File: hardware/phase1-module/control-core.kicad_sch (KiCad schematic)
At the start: 17 parts, among them U1 DAC80502, U2 OPA2189

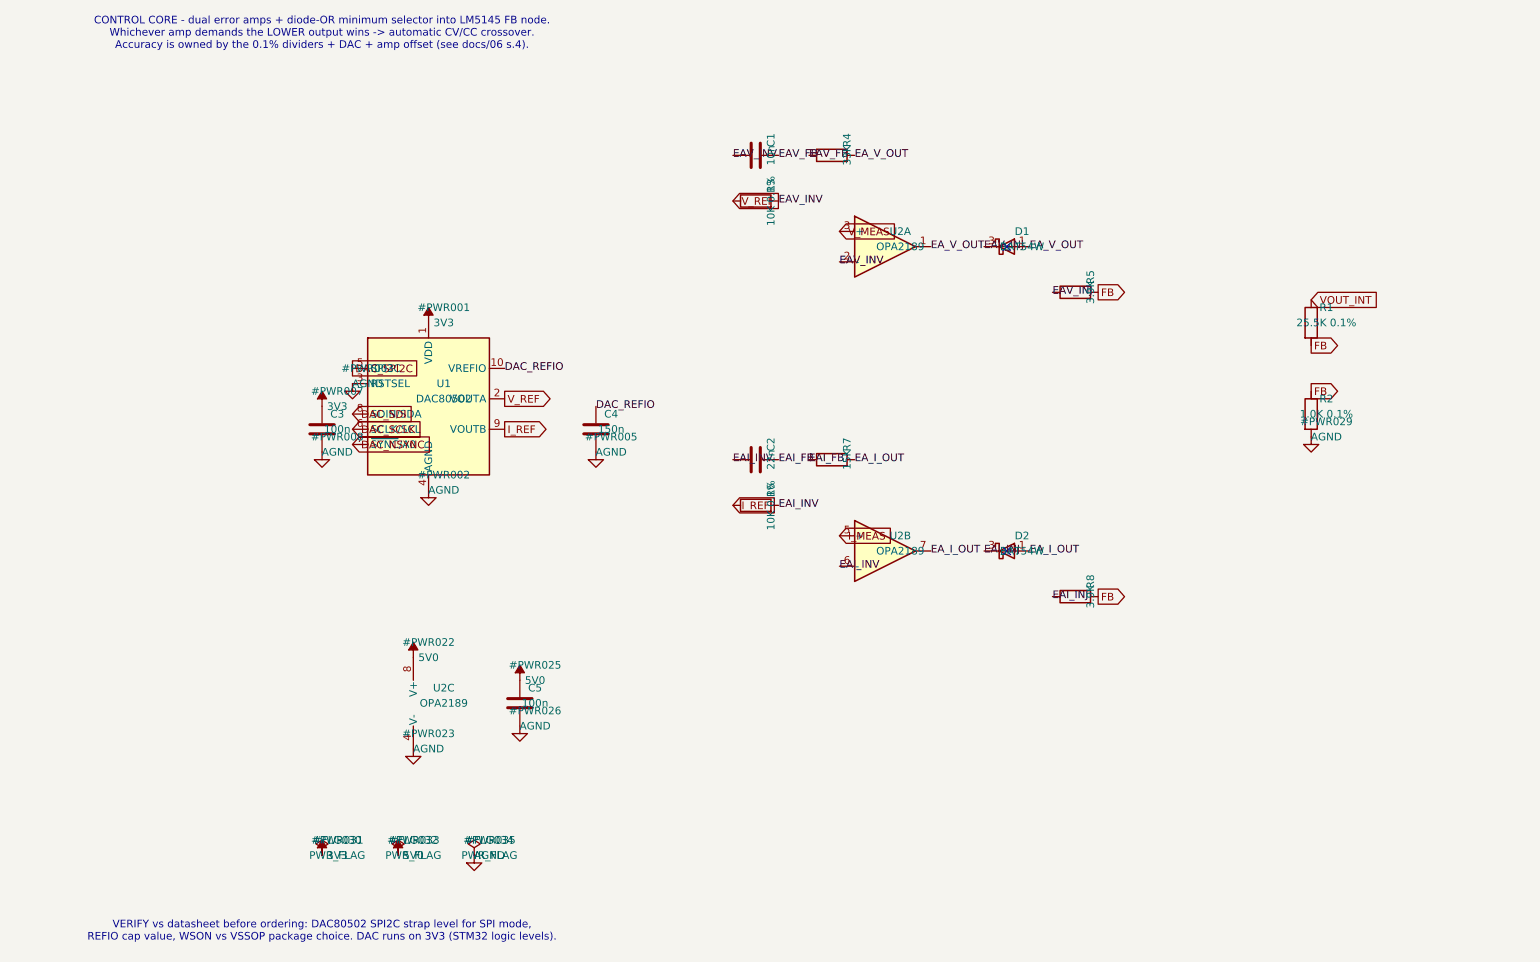
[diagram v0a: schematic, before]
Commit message: control-core sheet: verified generation, wired runs, clean field placement
- kicad_gen: pin-bbox-based Reference/Value placement, wire support,
  outward-rotated labels, synthesized power ports, hidden flag text
- gen_phase1: control-core rows rewired (op-amp -> diode-OR -> injection
  as real wires with on-wire labels), collision fixes, DAC decoupling moved
- Netlist assertions pass 22/22 (check_netlist.py); render inspected
- docs/06: DAC80502 moved to 3V3 rail (STM32 logic levels), BAT54W SC-70
  pinout notes

Co-Authored-By: Claude Fable 5 <noreply@anthropic.com>
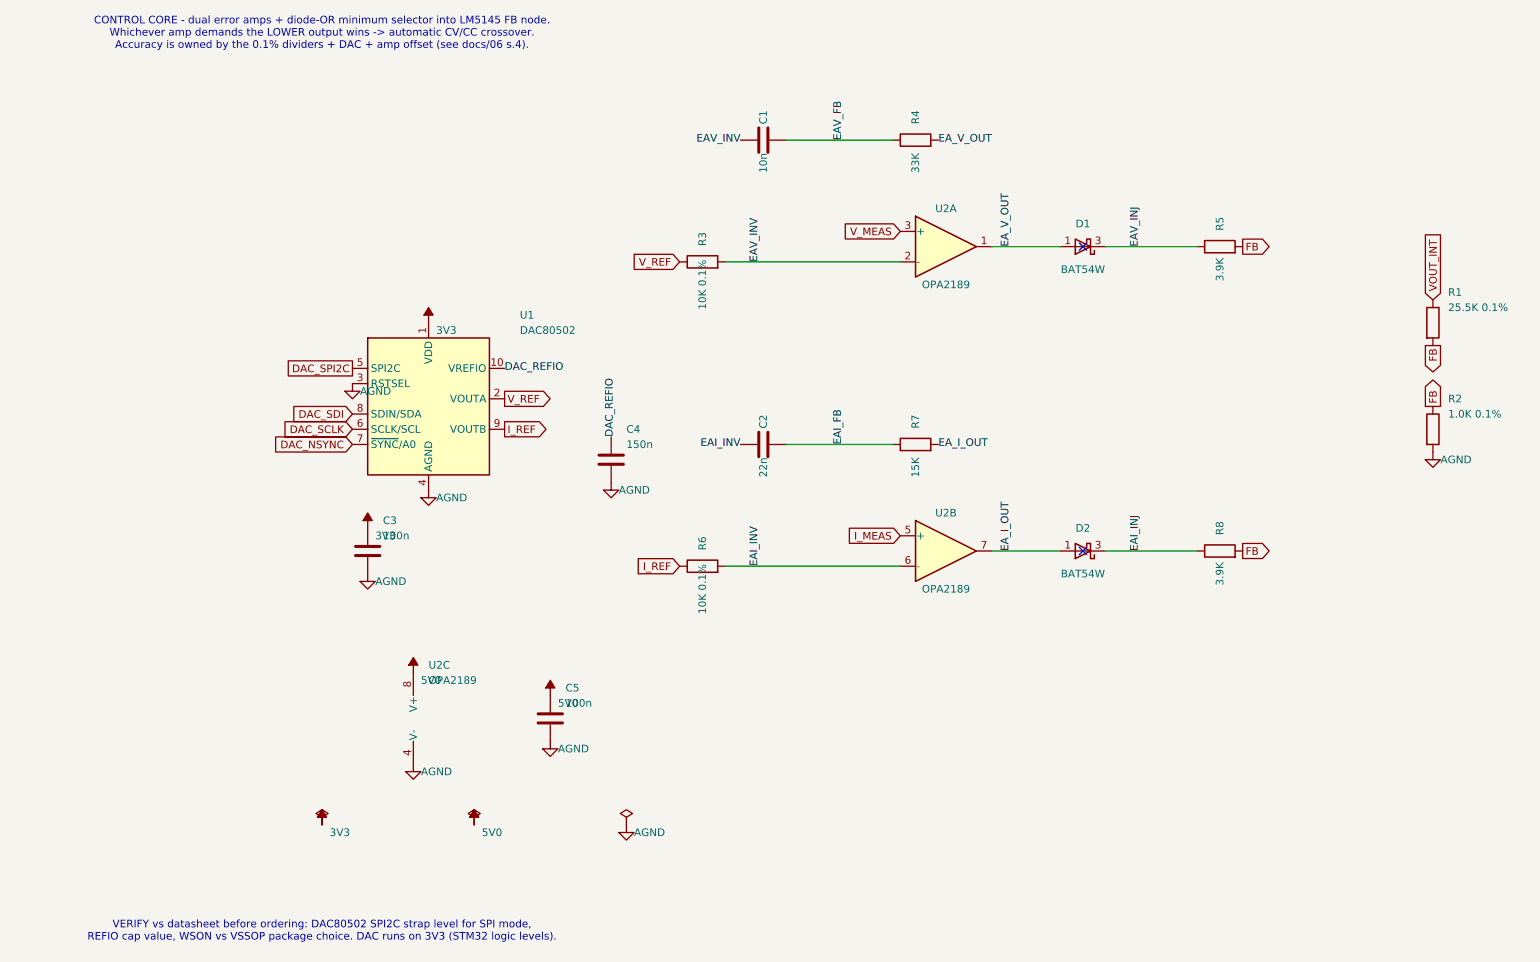
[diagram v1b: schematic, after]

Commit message: Two part disqualifications caught by exact-variant spec check
- OPA2189 -> OPA2333: OPAx189 input common-mode range stops ~2.5V below
  V+, colliding with our 2.5V full-scale signals on the 5V rail
- TPS54202 -> LMR36015: 28V Vin(max) is inside the 24-30V bus spec;
  60V part restores margin
- DAC80502 footprint pinned to VSSOP-10 (DGS), exact orderables for all
  section-B parts in PARTS-TO-DOWNLOAD.md (incl. STM32G431CBT6 + RM0440)

Co-Authored-By: Claude Fable 5 <noreply@anthropic.com>
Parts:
- U1: footprint Package_SON:WSON-10-1EP_2.5x2.5mm_P0.5mm -> Package_SO:VSSOP-10_3x3mm_P0.5mm
- U2: value OPA2189 -> OPA2333
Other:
- note added: "VERIFY vs datasheet before ordering: DAC80502 SPI2C strap level for SPI mode, REFIO cap value. Package: VSSOP-10 (DGS). DAC runs on 3V3 (STM32 logic levels). EAs: OPA2333 (RRIO; OPA2189 rejected - input CM stops 2.5V below V+)."
- note removed: "VERIFY vs datasheet before ordering: DAC80502 SPI2C strap level for SPI mode, REFIO cap value, WSON vs VSSOP package choice. DAC runs on 3V3 (STM32 logic levels)."
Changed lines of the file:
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@@
   (global_label "FB" (shape output) (at 218.44 102.87 90) (fields_autoplaced) (effects (font (size 1.27 1.27))))
   (text "CONTROL CORE - dual error amps + diode-OR minimum selector into LM5145 FB node.\nWhichever amp demands the LOWER output wins -> automatic CV/CC crossover.\nAccuracy is owned by the 0.1% dividers + DAC + amp offset (see docs/06 s.4)." (at 33.02 40.64 0) (effects (font (size 1.27 1.27))))
-  (text "VERIFY vs datasheet before ordering: DAC80502 SPI2C strap level for SPI mode,\nREFIO cap value, WSON vs VSSOP package choice. DAC runs on 3V3 (STM32 logic levels)." (at 33.02 190.5 0) (effects (font (size 1.27 1.27))))
+  (text "VERIFY vs datasheet before ordering: DAC80502 SPI2C strap level for SPI mode,\nREFIO cap value. Package: VSSOP-10 (DGS). DAC runs on 3V3 (STM32 logic levels).\nEAs: OPA2333 (RRIO; OPA2189 rejected - input CM stops 2.5V below V+)." (at 33.02 190.5 0) (effects (font (size 1.27 1.27))))
   (symbol (lib_id "Analog_DAC:DAC80502") (at 50.8 101.6 0) (unit 1)
     (in_bom yes) (on_board yes) (dnp no)
     (property "Reference" "U1" (at 66.04 87.63000000000001 0) (effects (font (size 1.27 1.27)) (justify left)))
     (property "Value" "DAC80502" (at 66.04 90.17 0) (effects (font (size 1.27 1.27)) (justify left)))
-    (property "Footprint" "Package_SON:WSON-10-1EP_2.5x2.5mm_P0.5mm" (at 50.8 101.6 0) (effects (font (size 1.27 1.27)) hide))
+    (property "Footprint" "Package_SO:VSSOP-10_3x3mm_P0.5mm" (at 50.8 101.6 0) (effects (font (size 1.27 1.27)) hide))
     (property "Datasheet" "~" (at 50.8 101.6 0) (effects (font (size 1.27 1.27)) hide))
     (pin "1")
@@
     (in_bom yes) (on_board yes) (dnp no)
     (property "Reference" "U2" (at 137.16 69.85 0) (effects (font (size 1.27 1.27))))
-    (property "Value" "OPA2189" (at 137.16 82.55 0) (effects (font (size 1.27 1.27))))
+    (property "Value" "OPA2333" (at 137.16 82.55 0) (effects (font (size 1.27 1.27))))
     (property "Footprint" "Package_SO:VSSOP-8_3x3mm_P0.65mm" (at 137.16 76.2 0) (effects (font (size 1.27 1.27)) hide))
     (property "Datasheet" "~" (at 137.16 76.2 0) (effects (font (size 1.27 1.27)) hide))
@@
     (in_bom yes) (on_board yes) (dnp no)
     (property "Reference" "U2" (at 137.16 120.64999999999999 0) (effects (font (size 1.27 1.27))))
-    (property "Value" "OPA2189" (at 137.16 133.35 0) (effects (font (size 1.27 1.27))))
+    (property "Value" "OPA2333" (at 137.16 133.35 0) (effects (font (size 1.27 1.27))))
     (property "Footprint" "Package_SO:VSSOP-8_3x3mm_P0.65mm" (at 137.16 127.0 0) (effects (font (size 1.27 1.27)) hide))
     (property "Datasheet" "~" (at 137.16 127.0 0) (effects (font (size 1.27 1.27)) hide))
@@
     (in_bom yes) (on_board yes) (dnp no)
     (property "Reference" "U2" (at 50.8 146.04999999999998 0) (effects (font (size 1.27 1.27)) (justify left)))
-    (property "Value" "OPA2189" (at 50.8 148.59 0) (effects (font (size 1.27 1.27)) (justify left)))
+    (property "Value" "OPA2333" (at 50.8 148.59 0) (effects (font (size 1.27 1.27)) (justify left)))
     (property "Footprint" "Package_SO:VSSOP-8_3x3mm_P0.65mm" (at 50.8 154.94 0) (effects (font (size 1.27 1.27)) hide))
     (property "Datasheet" "~" (at 50.8 154.94 0) (effects (font (size 1.27 1.27)) hide))

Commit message: DAC80502 straps verified and applied; two package corrections
- SPI2C strapped to AGND (low = SPI mode, ds 8.5.1); RSTSEL low =
  zero-code POR confirmed - both now hardwired in control-core
- DAC80502 is WSON-10 (DRX) only; VSSOP/DGS was the DAC80501 single.
  Footprint reverted, Value = DAC80502DRXT
- LMR36015 is VQFN-HR-12 (RNX), not HSOIC-8; AQRNXRQ1 variant vetted
  (adjustable, 400 kHz, non-FPWM) and merged for the aux-rails sheet
- Netlist: 21 nets pass (DAC_SPI2C net absorbed into AGND)

Co-Authored-By: Claude Fable 5 <noreply@anthropic.com>
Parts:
- U1: value DAC80502 -> DAC80502DRXT; footprint Package_SO:VSSOP-10_3x3mm_P0.5mm -> Package_SON:WSON-10-1EP_2.5x2.5mm_P0.5mm
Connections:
- net DAC_SPI2C is gone; now on net AGND: U1.5 (SPI2C)
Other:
- note added: "DAC80502DRXT (WSON-10): SPI2C->AGND = SPI mode; RSTSEL->AGND = zero-code POR (both verified vs datasheet). DAC runs on 3V3 = STM32 IO rail (IOVDD<=VDD rule). EAs: OPA2333 (RRIO; OPA2189 rejected - input CM stops 2.5V below V+)."
- note removed: "VERIFY vs datasheet before ordering: DAC80502 SPI2C strap level for SPI mode, REFIO cap value. Package: VSSOP-10 (DGS). DAC runs on 3V3 (STM32 logic levels). EAs: OPA2333 (RRIO; OPA2189 rejected - input CM stops 2.5V below V+)."

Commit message: Footprint pass: labbench.pretty library, all 137 components verified
- build_fplib.py: merges vetted vendor footprints (LM5145 RGY0020B,
  LMR36015 RNX, DAC80502 WSON-10 no-EP) and generates PowerFET_SON5x6_GDS
  from the TI Q5A land pattern (CSD18563Q5A SLPS444C) with pads renumbered
  1=G/2=D/3=S to match the generic NMOS symbol; writes fp-lib-table.
- check_footprints.py: every component must have a resolvable footprint and
  every netted pin a matching pad (caught a wrong official VSSOP-8 name).
- gen_phase1.py: passives 0402->0603 (hand assembly); DAC80502 vendor fp
  (DRX has no exposed pad); L1 = Coilcraft XAL1350-103ME on official fp;
  net-tie fp; crystal -> Crystal_GND24 with grounded shield pads; bulk cap
  banks expanded to one component per physical cap (C75-C81); R27 preload
  1W -> 2512.
- PARTS-TO-DOWNLOAD.md section D: new orderables for the footprint pass.

check_netlist + check_footprints: all OK (137 components).

Co-Authored-By: Claude Fable 5 <noreply@anthropic.com>
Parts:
- C1, C2, C3, C4, C5: footprint Capacitor_SMD:C_0402_1005Metric -> Capacitor_SMD:C_0603_1608Metric
- R1, R2, R3, R4, R5, R6, R7, R8: footprint Resistor_SMD:R_0402_1005Metric -> Resistor_SMD:R_0603_1608Metric
- U1: footprint Package_SON:WSON-10-1EP_2.5x2.5mm_P0.5mm -> labbench:DAC80502_DRX_WSON-10
- U2: footprint Package_SO:VSSOP-8_3x3mm_P0.65mm -> Package_SO:VSSOP-8_3.0x3.0mm_P0.65mm
